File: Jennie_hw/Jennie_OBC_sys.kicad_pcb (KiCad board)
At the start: 2 copper layers, 80 x 80 mm, 28 parts, among them IC1 TPS79533DCQ, J5 Conn_01x10, J6 Conn_01x15, SW2 SW_MEC_5E, SW3 SW_MEC_5E, U1 ATmega328PB-A, Y1 16MHz

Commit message: Jennie and Jára PCBs prepared for manufacturing(?)
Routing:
- net (no net): vias 0 -> 3
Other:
- board text added: "JENNIE-OBC:BOTTOM"
- board text added: "JENNIE-OBC:TOP"
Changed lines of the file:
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@@
 			)
 		)
+		(model "C:/Users/Uživatel/Documents/MPA-NDE/kicad_project_libs/push_btn/1571527-2.stp"
+			(offset
+				(xyz 0 0 3.7)
+			)
+			(scale
+				(xyz 1 1 1)
+			)
+			(rotate
+				(xyz 0 0 0)
+			)
+		)
 	)
 	(footprint "Resistor_SMD:R_0805_2012Metric"
@@
 		(tags "Through hole pin header THT 1x02 2.54mm single row")
 		(property "Reference" "J1"
-			(at 0 -2.33 360)
+			(at 0 -2.33 0)
 			(layer "F.SilkS")
 			(effects
@@
 		)
 		(property "Value" "~"
-			(at 0 4.87 360)
+			(at 0 4.87 0)
 			(layer "F.Fab")
 			(effects
@@
 			)
 		)
+		(model "C:/Users/Uživatel/Documents/MPA-NDE/kicad_project_libs/push_btn/1571527-2.stp"
+			(offset
+				(xyz 0 0 3.7)
+			)
+			(scale
+				(xyz 1 1 1)
+			)
+			(rotate
+				(xyz 0 0 0)
+			)
+		)
 	)
 	(footprint "Capacitor_SMD:C_0805_2012Metric"
@@
 		)
 		(fp_text user "${REFERENCE}"
-			(at 1.25 0 360)
+			(at 1.25 0 0)
 			(layer "F.Fab")
 			(effects
@@
 		)
 	)
+	(gr_line
+		(start 110.34 138.24)
+		(end 114.86 138.24)
+		(stroke
+			(width 0.6)
+			(type default)
+		)
+		(layer "Dwgs.User")
+	)
+	(gr_line
+		(start 110.36 57.54)
+		(end 110.36 62.06)
+		(stroke
+			(width 0.6)
+			(type default)
+		)
+		(layer "Dwgs.User")
+	)
+	(gr_line
+		(start 115.11 57.54)
+		(end 110.36 57.54)
+		(stroke
+			(width 0.6)
+			(type default)
+		)
+		(layer "Dwgs.User")
+	)
+	(gr_line
+		(start 191.05 57.53)
+		(end 186.53 57.53)
+		(stroke
+			(width 0.6)
+			(type default)
+		)
+		(layer "Dwgs.User")
+	)
+	(gr_line
+		(start 191.05 138.23)
+		(end 191.05 133.71)
+		(stroke
+			(width 0.6)
+			(type default)
+		)
+		(layer "Dwgs.User")
+	)
+	(gr_line
+		(start 110.34 133.49)
+		(end 110.34 138.24)
+		(stroke
+			(width 0.6)
+			(type default)
+		)
+		(layer "Dwgs.User")
+	)
+	(gr_line
+		(start 191.05 62.28)
+		(end 191.05 57.53)
+		(stroke
+			(width 0.6)
+			(type default)
+		)
+		(layer "Dwgs.User")
+	)
+	(gr_line
+		(start 186.3 138.23)
+		(end 191.05 138.23)
+		(stroke
+			(width 0.6)
+			(type default)
+		)
+		(layer "Dwgs.User")
+	)
 	(gr_rect
 		(start 110.7 57.88)
@@
 		)
 	)
+	(gr_text "JENNIE-OBC:TOP"
+		(at 141.55 56.64 0)
+		(layer "F.Cu")
+		(effects
+			(font
+				(size 1.5 1.5)
+				(thickness 0.375)
+				(bold yes)
+			)
+			(justify left bottom)
+		)
+	)
+	(gr_text "JENNIE-OBC:BOTTOM"
+		(at 163.53 54.1 -0)
+		(layer "B.Cu")
+		(effects
+			(font
+				(size 1.5 1.5)
+				(thickness 0.3)
+				(bold yes)
+			)
+			(justify left bottom mirror)
+		)
+	)
+	(dimension
+		(type center)
+		(layer "Dwgs.User")
+		(pts
+			(xy 109.7 138.88) (xy 109.7 148.17)
+		)
+		(style
+			(thickness 1)
+			(arrow_length 1.27)
+			(text_position_mode 0)
+			(extension_offset 0.5) keep_text_aligned)
+	)
+	(dimension
+		(type center)
+		(layer "Dwgs.User")
+		(pts
+			(xy 191.69 56.88) (xy 201.2 56.88)
+		)
+		(style
+			(thickness 1)
+			(arrow_length 1.27)
+			(text_position_mode 0)
+			(extension_offset 0.5) keep_text_aligned)
+	)
+	(dimension
+		(type center)
+		(layer "Dwgs.User")
+		(pts
+			(xy 109.71 56.9) (xy 109.71 65.07)
+		)
+		(style
+			(thickness 1)
+			(arrow_length 1.27)
+			(text_position_mode 0)
+			(extension_offset 0.5) keep_text_aligned)
+	)
+	(via
+		(at 191.69 56.88)
+		(size 1.5)
+		(drill 0.6)
+		(layers "F.Cu" "B.Cu")
+		(net 0)
+	)
+	(via
+		(at 109.69 138.88)
+		(size 1.5)
+		(drill 0.6)
+		(layers "F.Cu" "B.Cu")
+		(net 0)
+	)
+	(via
+		(at 109.69 56.88)
+		(size 1.5)
+		(drill 0.6)
+		(layers "F.Cu" "B.Cu")
+		(net 0)
+	)
 	(segment

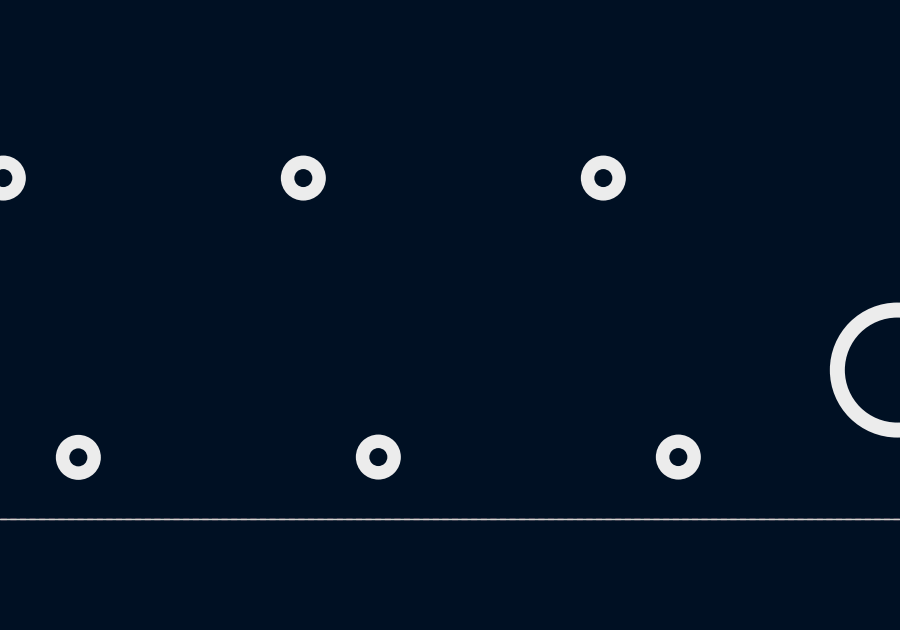
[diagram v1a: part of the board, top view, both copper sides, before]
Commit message: 3D models of Jára and Jennie PCBs added
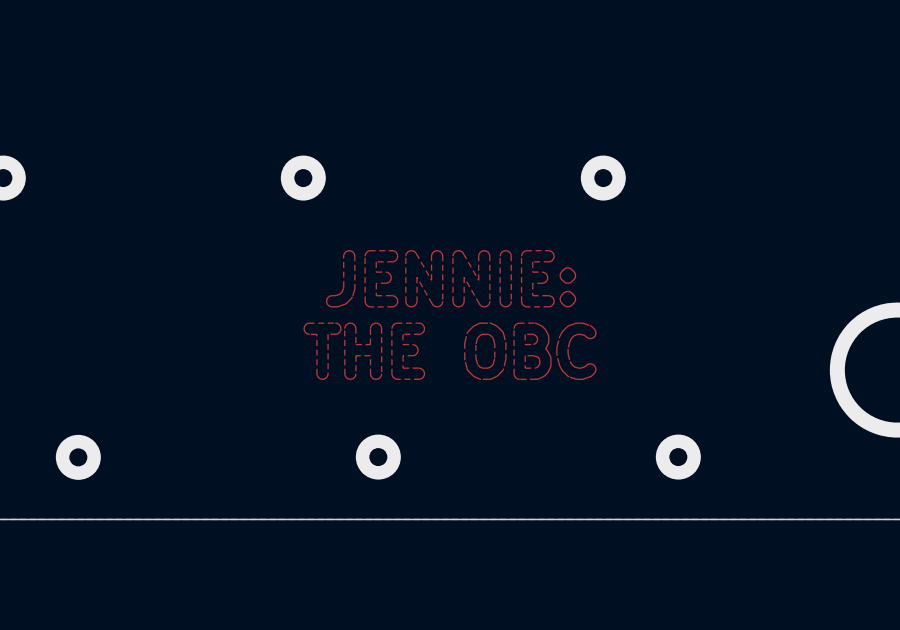
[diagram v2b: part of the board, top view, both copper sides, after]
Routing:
- added copper zone on F.Cu, net (none)

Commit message: Push buttons moved to bottom side, STEP model of TP4056 added
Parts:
- SW2, SW3: moved to B.Cu
- moved SW3 3.92 mm to (177.3, 112.1), turned to 0 degrees
- turned SW2 to 0 degrees
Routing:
- net /BTN1: track 16.1 -> 21.6 mm, vias 0 -> 1
- net /RST: track 31.5 -> 32.6 mm, vias 1 -> 2

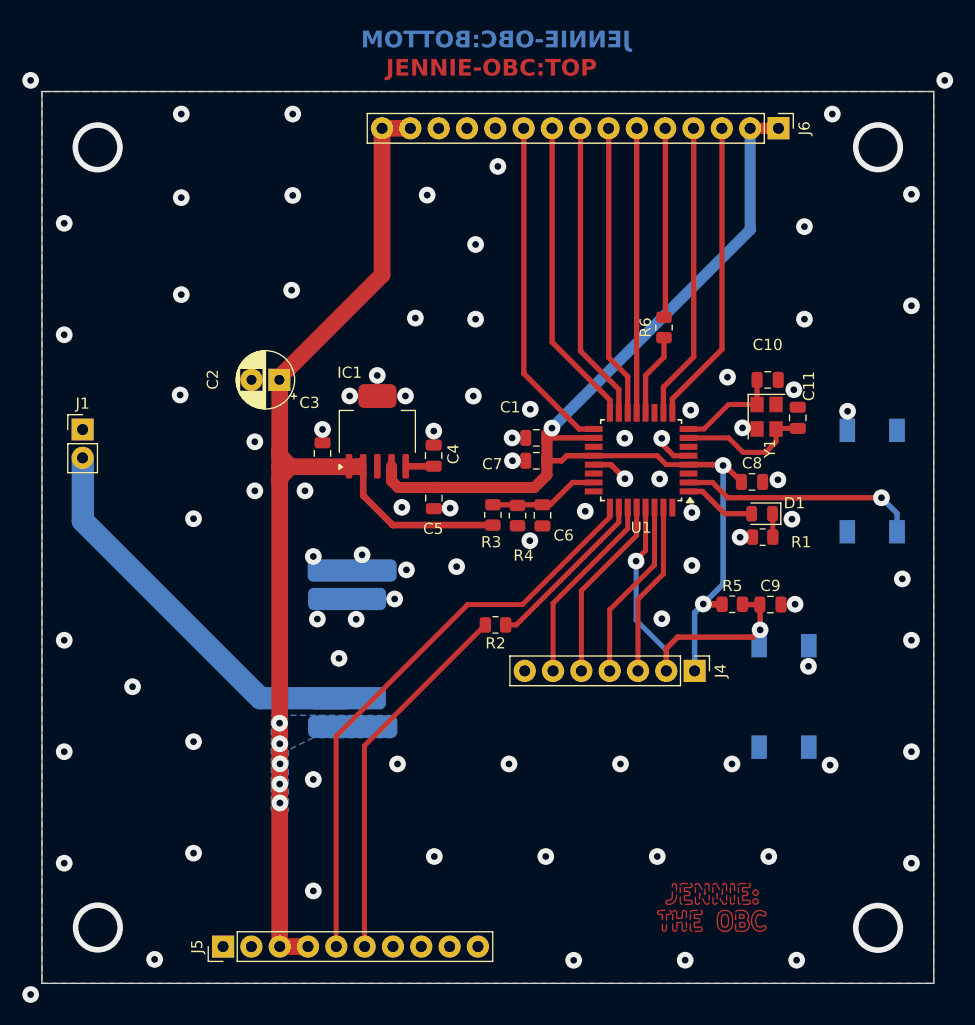
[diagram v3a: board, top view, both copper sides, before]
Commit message: remove before start switch added
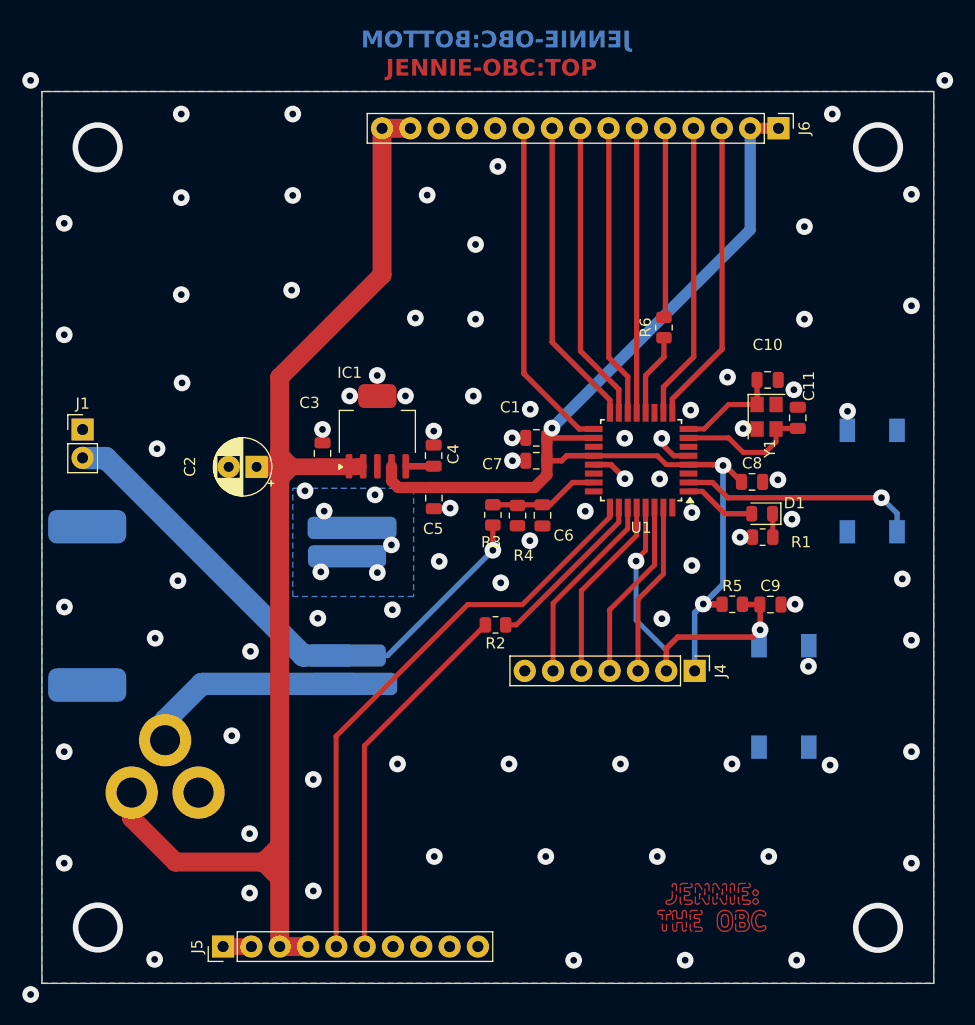
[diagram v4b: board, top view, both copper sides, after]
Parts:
- added J2: Barrel_Jack_Switch, Connector_BarrelJack:BarrelJack_Horizontal, B.Cu at (124.8, 120.8)
- SW2: value SW_MEC_5E -> (none)
- U2: value ~ -> TP4056 charger module
- moved C2 8.07 mm to (130.0, 91.5)
- moved U2 3.83 mm to (125.3, 104.0)
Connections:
- R3 pad 2: V_OUT -> V_BATT
- U2 pad 3: V_OUT -> OUT+
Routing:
- net OUT+: track 0.00 -> 19.9 mm
- net V_BATT: track 35.9 -> 50.3 mm, vias 0 -> 1
- net V_OUT: track 108.0 -> 116.5 mm, vias 5 -> 0
- net GND: track 6.69 -> 9.23 mm, vias 90 -> 91
- removed copper zone on B.Cu, net V_OUT

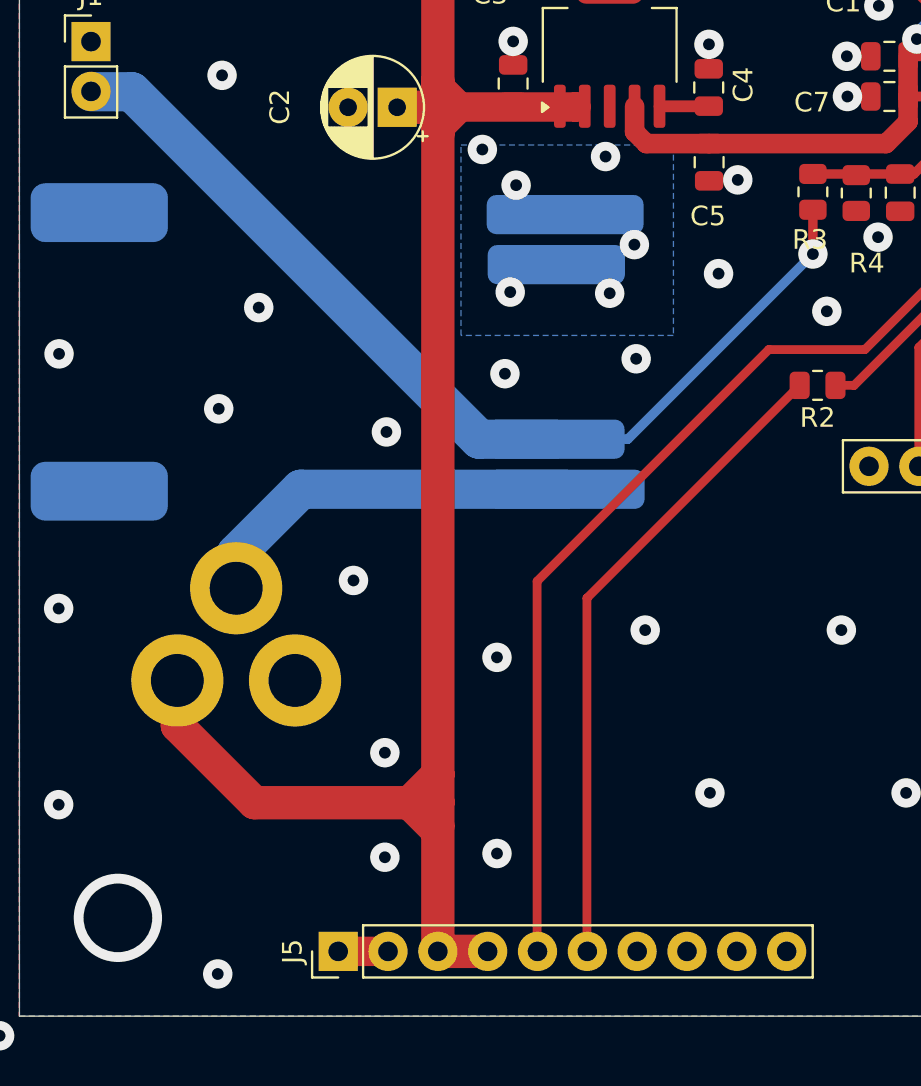
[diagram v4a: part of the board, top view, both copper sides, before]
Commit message: small fix of small routing error on Jennie PCB (V_batt routed to different pins on pinheader to maintain compatibility with Jára pinheader)
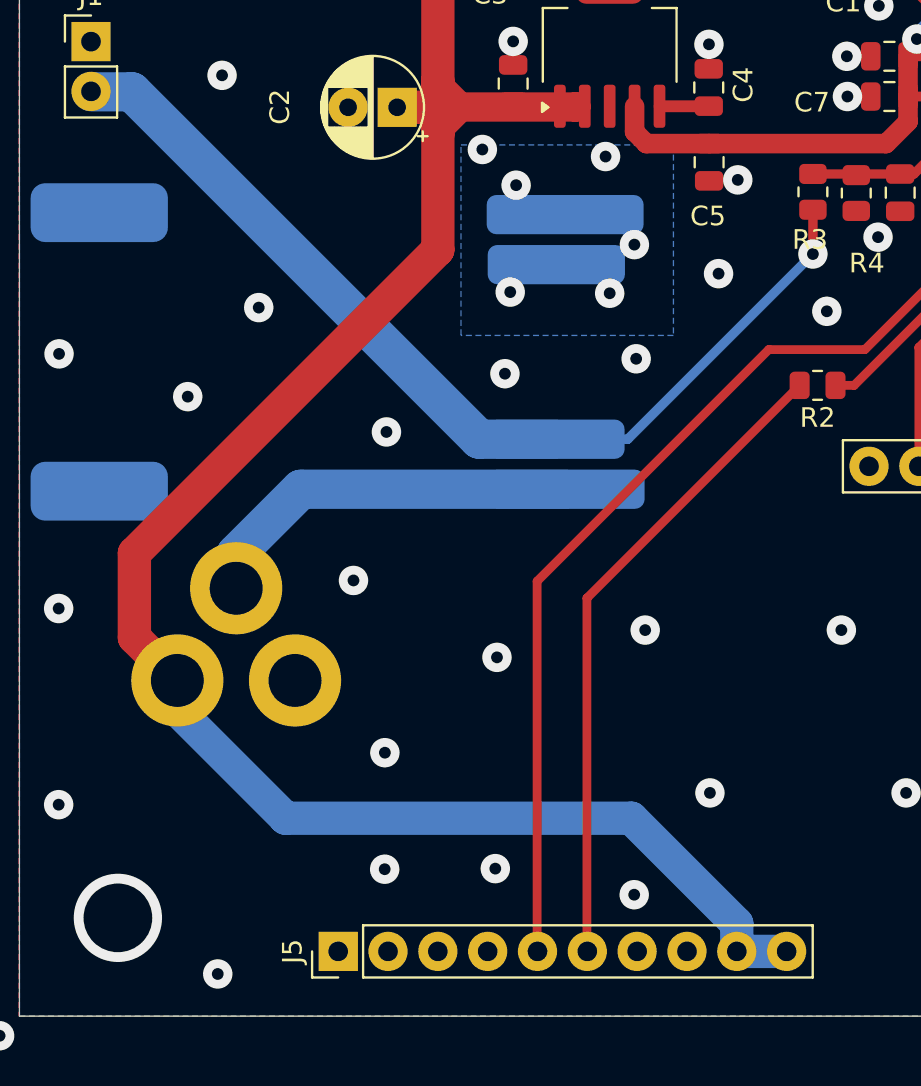
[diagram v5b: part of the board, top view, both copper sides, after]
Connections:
- J5 pad 10: GND -> V_OUT
- J5 pad 3: V_OUT -> GND
- J5 pad 4: V_OUT -> GND
- J5 pad 9: GND -> V_OUT
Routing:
- net V_OUT: track 116.5 -> 124.8 mm
- net GND: track 9.23 -> 6.69 mm, vias 91 -> 92
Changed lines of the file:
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@@
 			(layers "*.Cu" "*.Mask")
 			(remove_unused_layers no)
-			(net 37 "V_OUT")
+			(net 2 "GND")
 			(pinfunction "Pin_3")
 			(pintype "passive")
@@
 			(layers "*.Cu" "*.Mask")
 			(remove_unused_layers no)
-			(net 37 "V_OUT")
+			(net 2 "GND")
 			(pinfunction "Pin_4")
 			(pintype "passive")
@@
 			(layers "*.Cu" "*.Mask")
 			(remove_unused_layers no)
-			(net 2 "GND")
+			(net 37 "V_OUT")
 			(pinfunction "Pin_9")
 			(pintype "passive")
@@
 			(layers "*.Cu" "*.Mask")
 			(remove_unused_layers no)
-			(net 2 "GND")
+			(net 37 "V_OUT")
 			(pinfunction "Pin_10")
 			(pintype "passive")
@@
 			(layers "B.Cu" "B.Paste" "B.Mask")
 			(roundrect_rratio 0.25)
-			(pinfunction "BATT+")
-			(pintype "input")
 			(thermal_bridge_angle 45)
 		)
@@
 			(layers "B.Cu" "B.Paste" "B.Mask")
 			(roundrect_rratio 0.25)
-			(pinfunction "BATT+")
-			(pintype "input")
 			(thermal_bridge_angle 45)
 		)
@@
 		(tags "Power Jack")
 		(property "Reference" "J2"
-			(at -8.45 -5.75 360)
+			(at -8.45 -5.75 0)
 			(layer "B.SilkS")
 			(effects
@@
 		)
 		(property "Value" "Barrel_Jack_Switch"
-			(at -6.2 5.5 360)
+			(at -6.2 5.5 0)
 			(layer "B.Fab")
 			(effects
@@
 		)
 		(fp_text user "${REFERENCE}"
-			(at -3 2.95 360)
+			(at -3 2.95 0)
 			(layer "B.Fab")
 			(effects
@@
 	)
 	(segment
-		(start 129.49 134.58)
-		(end 126.95 134.58)
-		(width 1.5)
-		(layer "F.Cu")
-		(net 2)
-	)
-	(segment
 		(start 161.74 91.35)
 		(end 163 92.61)
@@
 	)
 	(via
-		(at 135.045 129.59)
+		(at 134.96 130.36)
 		(size 1.5)
 		(drill 0.6)
@@
 	)
 	(via
+		(at 142.04 131.69)
+		(size 1.5)
+		(drill 0.6)
+		(layers "F.Cu" "B.Cu")
+		(free yes)
+		(net 2)
+	)
+	(via
 		(at 123.2 67.4)
 		(size 1.5)
@@
 	)
 	(via
-		(at 120.86 106.92)
+		(at 119.28 106.3)
 		(size 1.5)
 		(drill 0.6)
@@
 	)
 	(via
-		(at 129.33 129.78)
+		(at 129.32 130.39)
 		(size 1.5)
 		(drill 0.6)
@@
 	)
 	(segment
-		(start 132.03 125.56)
-		(end 132.03 92.93)
-		(width 1.7)
-		(layer "F.Cu")
-		(net 37)
-	)
-	(segment
-		(start 130.59 127)
-		(end 131.83 128.24)
-		(width 1.7)
-		(layer "F.Cu")
-		(net 37)
-	)
-	(segment
 		(start 141.21 61.18)
 		(end 143.75 61.18)
@@
 	)
 	(segment
-		(start 122.68 127)
-		(end 130.37 127)
-		(width 1.7)
-		(layer "F.Cu")
-		(net 37)
-	)
-	(segment
 		(start 132.03 92.93)
 		(end 132.03 92.525)
@@
 	)
 	(segment
-		(start 132.03 126.98)
-		(end 132.03 125.56)
-		(width 1.7)
-		(layer "F.Cu")
-		(net 37)
-	)
-	(segment
 		(start 132.03 92.525)
 		(end 133 91.555)
@@
 	)
 	(segment
-		(start 132.03 134.58)
-		(end 132.03 128.18)
+		(start 141.21 74.33)
+		(end 141.21 61.18)
 		(width 1.7)
 		(layer "F.Cu")
@@
 	)
 	(segment
-		(start 141.21 74.33)
-		(end 141.21 61.18)
+		(start 132.03 83.51)
+		(end 141.21 74.33)
 		(width 1.7)
 		(layer "F.Cu")
@@
 	)
 	(segment
-		(start 132.03 83.51)
-		(end 141.21 74.33)
+		(start 116.56 118.5775)
+		(end 116.56 114.28)
 		(width 1.7)
 		(layer "F.Cu")
@@
 	)
 	(segment
-		(start 133 91.535)
-		(end 139.065 91.535)
-		(width 1.5)
+		(start 132.03 98.81)
+		(end 132.03 92.93)
+		(width 1.7)
 		(layer "F.Cu")
 		(net 37)
 	)
 	(segment
-		(start 132.03 134.58)
-		(end 134.57 134.58)
-		(width 1.7)
+		(start 133 91.535)
+		(end 139.065 91.535)
+		(width 1.5)
 		(layer "F.Cu")
 		(net 37)
@@
 	)
 	(segment
-		(start 132.03 128.18)
-		(end 132.03 126.98)
+		(start 118.75 120.7675)
+		(end 116.56 118.5775)
 		(width 1.7)
 		(layer "F.Cu")
@@
 	)
 	(segment
-		(start 118.75 123.07)
-		(end 122.68 127)
+		(start 132.03 91.535)
+		(end 132.03 90.19)
 		(width 1.7)
 		(layer "F.Cu")
@@
 	)
 	(segment
-		(start 132.01 127)
-		(end 132.03 126.98)
+		(start 132.03 91.535)
+		(end 133 91.535)
 		(width 1.7)
 		(layer "F.Cu")
@@
 	)
 	(segment
-		(start 130.37 127)
-		(end 132.01 127)
+		(start 116.56 114.28)
+		(end 132.03 98.81)
 		(width 1.7)
 		(layer "F.Cu")
@@
 	)
 	(segment
-		(start 132.03 91.535)
-		(end 132.03 90.19)
-		(width 1.7)
+		(start 139.065 91.535)
+		(end 139.07 91.53)
+		(width 1.5)
 		(layer "F.Cu")
 		(net 37)
 	)
 	(segment
-		(start 118.75 120.7675)
-		(end 118.75 123.07)
+		(start 124.27 127.79)
+		(end 141.894213 127.79)
 		(width 1.7)
-		(layer "F.Cu")
+		(layer "B.Cu")
 		(net 37)
 	)
 	(segment
-		(start 132.03 91.535)
-		(end 133 91.535)
+		(start 149.81 134.58)
+		(end 147.27 134.58)
 		(width 1.7)
-		(layer "F.Cu")
+		(layer "B.Cu")
 		(net 37)
 	)
 	(segment
-		(start 130.59 127)
-		(end 132.03 125.56)
+		(start 147.27 133.165787)
+		(end 147.27 134.58)
 		(width 1.7)
-		(layer "F.Cu")
+		(layer "B.Cu")
 		(net 37)
 	)
 	(segment
-		(start 130.37 127)
-		(end 130.59 127)
+		(start 141.894213 127.79)
+		(end 147.27 133.165787)
 		(width 1.7)
-		(layer "F.Cu")
+		(layer "B.Cu")
 		(net 37)
 	)
 	(segment
-		(start 139.065 91.535)
-		(end 139.07 91.53)
+		(start 118.75 122.27)
+		(end 124.27 127.79)
+		(width 1.7)
+		(layer "B.Cu")
+		(net 37)
+	)
+	(segment
+		(start 118.75 120.7675)
+		(end 118.75 122.27)
 		(width 1.5)
-		(layer "F.Cu")
+		(layer "B.Cu")
 		(net 37)
 	)
